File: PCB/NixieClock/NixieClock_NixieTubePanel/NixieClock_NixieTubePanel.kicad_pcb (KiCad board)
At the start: 2 copper layers, 112 x 112 mm, 30 parts, among them J3 Conn_01x04_Pin, J4 Conn_01x04_Pin, U1 K155ID1, U2 K155ID1, U3 K155ID1, U4 K155ID1, U5 PCF8574, U6 PCF8574, X1 5230, X2 5230, X3 5230, X4 5230, X5 5230, X6 5230

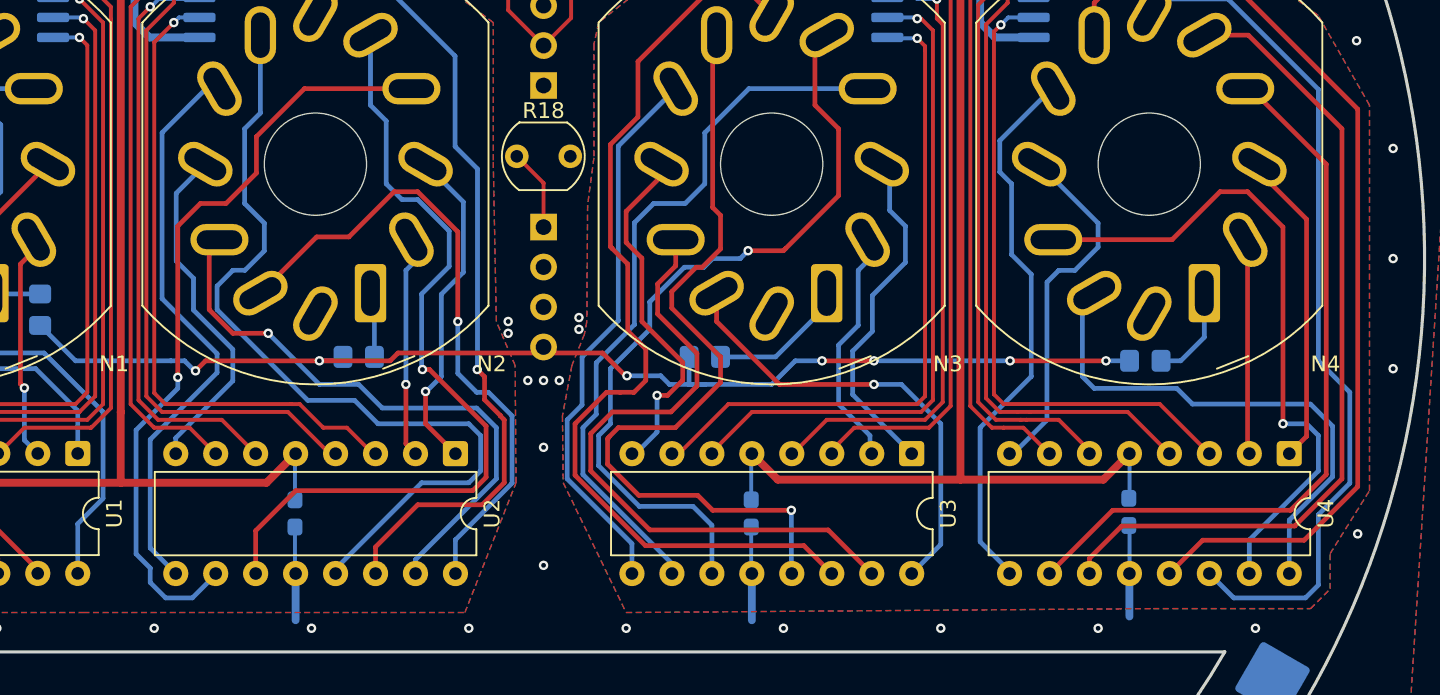
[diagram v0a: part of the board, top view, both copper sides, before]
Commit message: Tidied +170V trace slightly
some unnecessary diagonal lines were removed
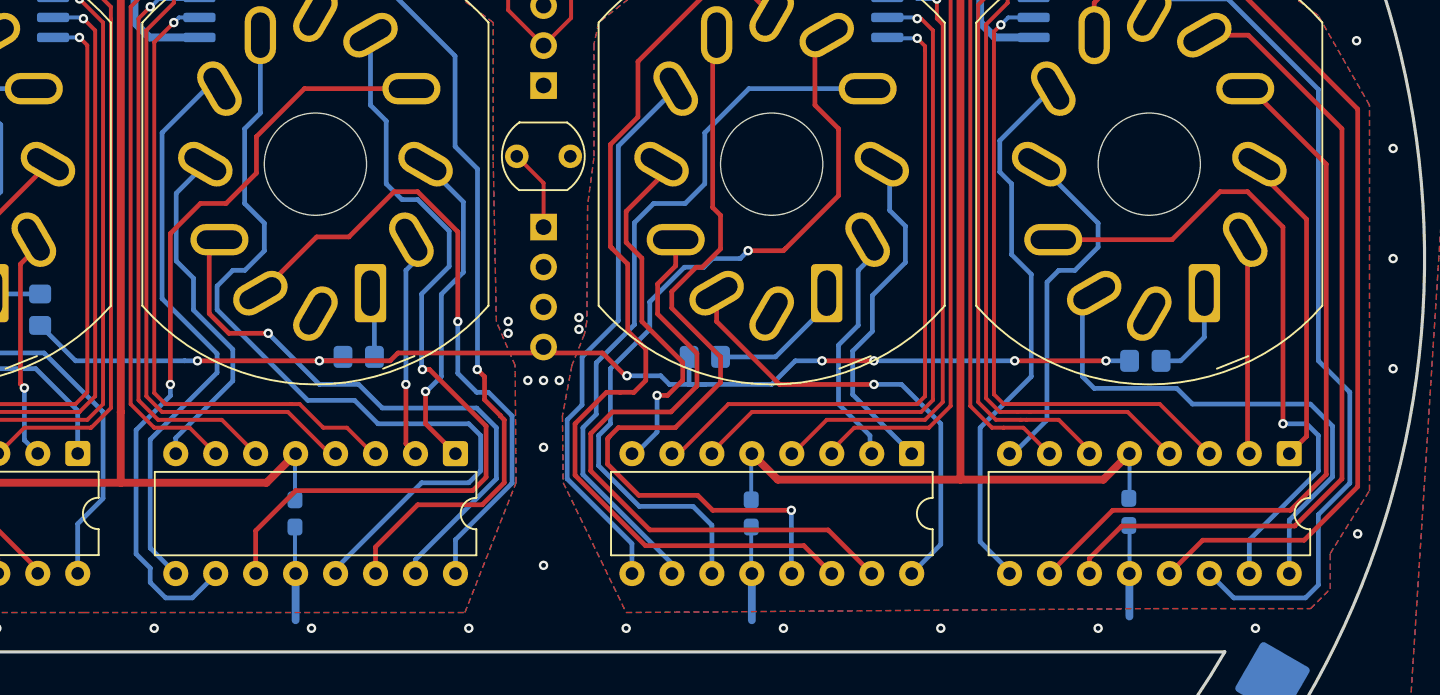
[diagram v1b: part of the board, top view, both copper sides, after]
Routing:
- net /+170V: track 78.5 -> 78.0 mm

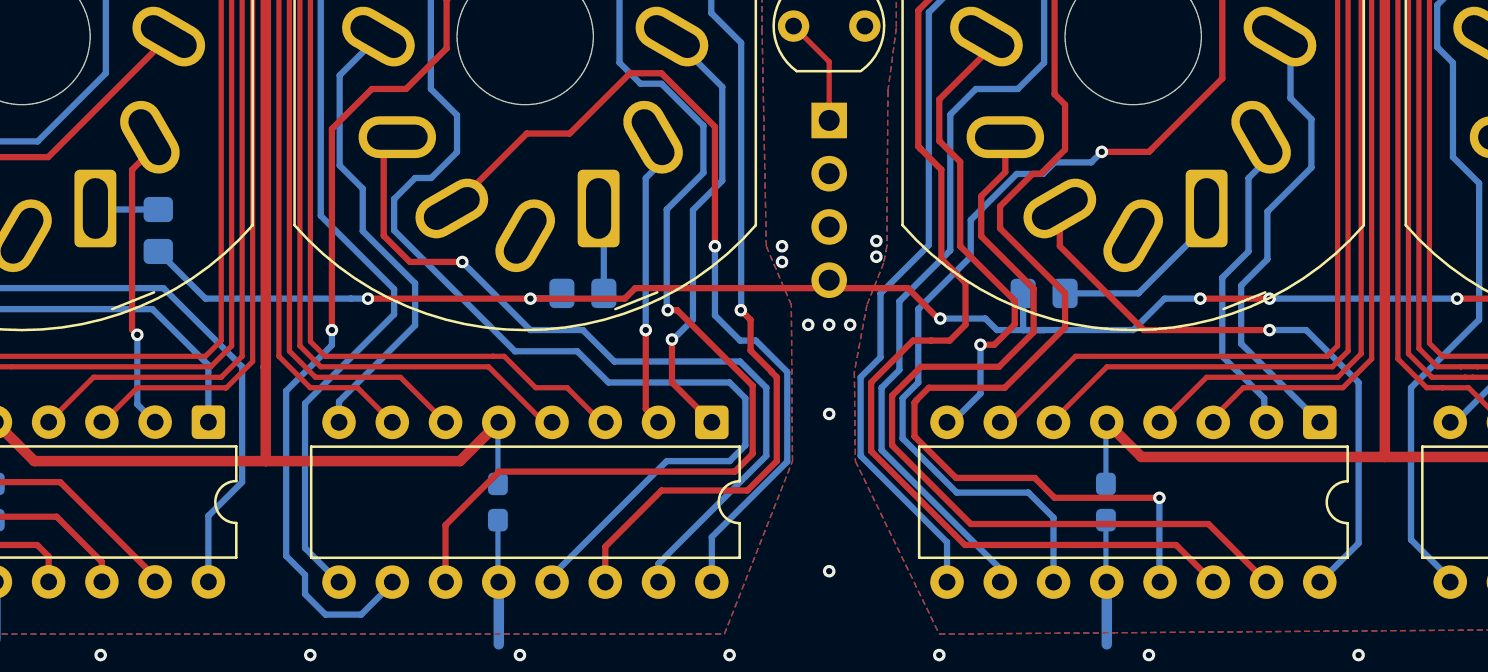
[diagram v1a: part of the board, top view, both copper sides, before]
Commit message: increase HV clearance on U3:8 trace
moved trace further from LV signals
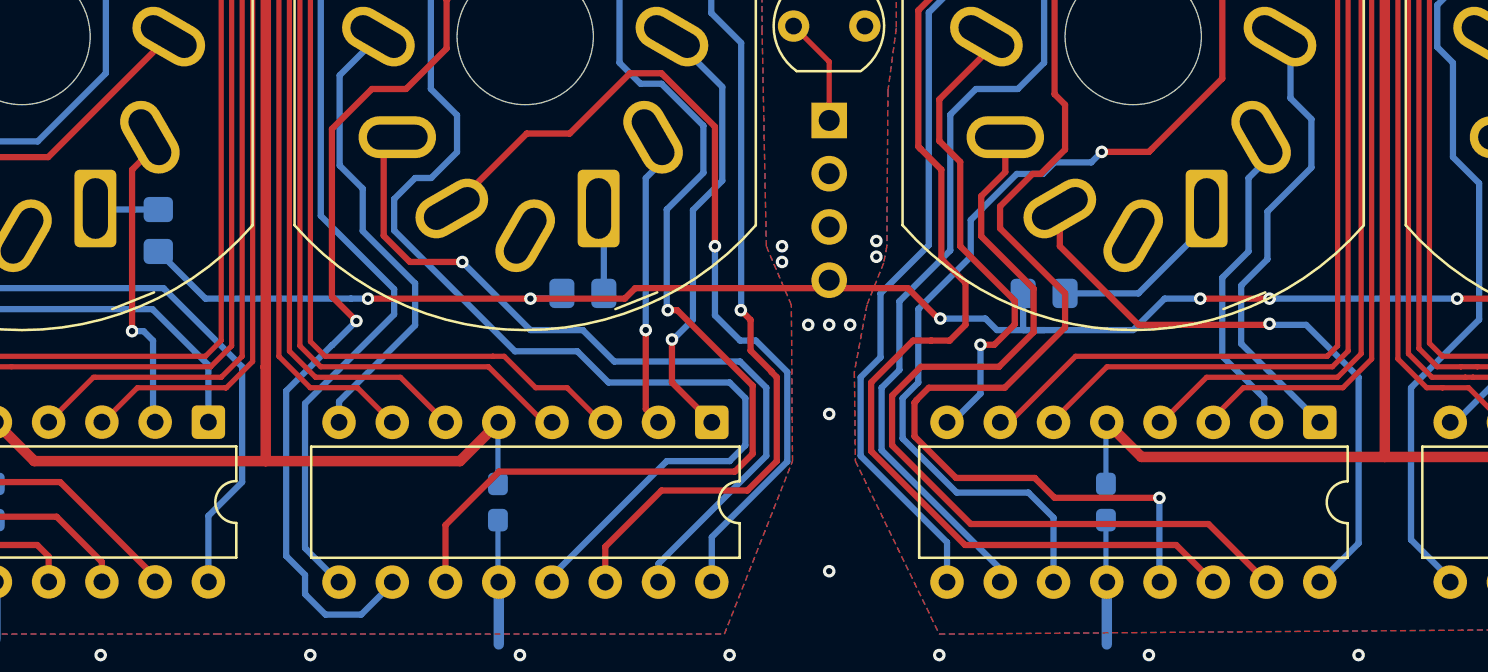
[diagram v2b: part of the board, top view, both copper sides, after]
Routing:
- net Net-(N2-'8'): track 49.3 -> 50.3 mm
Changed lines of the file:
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@@
 	)
 	(segment
-		(start 145 108)
+		(start 150.950003 107.75)
+		(end 144.75 107.75)
+		(width 0.3)
+		(layer "F.Cu")
+		(net 11)
+	)
+	(segment
+		(start 144.75 107.75)
 		(end 141 104)
 		(width 0.3)
@@
 	)
 	(segment
-		(start 151 108)
-		(end 145 108)
+		(start 151 107.700003)
+		(end 150.950003 107.75)
 		(width 0.3)
 		(layer "F.Cu")
@@
 	)
 	(via
-		(at 151 108)
+		(at 151 107.700003)
 		(size 0.6)
 		(drill 0.3)
@@
 	)
 	(segment
-		(start 152.75 108)
-		(end 155.25 110.5)
+		(start 155.25 118.17)
+		(end 153.4 120.02)
 		(width 0.3)
 		(layer "B.Cu")
@@
 	)
 	(segment
-		(start 155.25 118.17)
-		(end 153.4 120.02)
+		(start 155.25 110.25)
+		(end 155.25 118.17)
 		(width 0.3)
 		(layer "B.Cu")
@@
 	)
 	(segment
-		(start 155.25 110.5)
-		(end 155.25 118.17)
+		(start 152.75 107.75)
+		(end 155.25 110.25)
 		(width 0.3)
 		(layer "B.Cu")
@@
 	)
 	(segment
-		(start 151 108)
-		(end 152.75 108)
+		(start 151.049997 107.75)
+		(end 152.75 107.75)
+		(width 0.3)
+		(layer "B.Cu")
+		(net 11)
+	)
+	(segment
+		(start 151 107.700003)
+		(end 151.049997 107.75)
 		(width 0.3)
 		(layer "B.Cu")
@@
 	)
 	(segment
-		(start 97.6 99.501)
-		(end 97.6 98.8)
-		(width 0.3)
-		(layer "F.Cu")
-		(net 38)
-	)
-	(segment
-		(start 97 108.225)
-		(end 96.75 107.975)
+		(start 96.75 108.05)
+		(end 96.75 100.351)
 		(width 0.3)
 		(layer "F.Cu")
@@
 	)
 	(segment
-		(start 96.75 107.975)
-		(end 96.75 100.351)
+		(start 97.6 99.501)
+		(end 97.6 98.8)
 		(width 0.3)
 		(layer "F.Cu")
@@
 	)
 	(via
-		(at 97 108.225)
+		(at 96.75 108.05)
 		(size 0.6)
 		(drill 0.3)
@@
 	)
 	(segment
-		(start 97 111.54)
+		(start 97.75 112.29)
 		(end 97.85 112.39)
 		(width 0.3)
@@
 	)
 	(segment
-		(start 97 108.225)
-		(end 97 111.54)
+		(start 96.75 108.05)
+		(end 97.3 108.05)
+		(width 0.3)
+		(layer "B.Cu")
+		(net 38)
+	)
+	(segment
+		(start 97.3 108.05)
+		(end 97.75 108.5)
+		(width 0.3)
+		(layer "B.Cu")
+		(net 38)
+	)
+	(segment
+		(start 97.75 108.5)
+		(end 97.75 112.29)
 		(width 0.3)
 		(layer "B.Cu")
@@
 	)
 	(segment
-		(start 109.818507 96.5)
-		(end 111.75 94.568507)
+		(start 114.8 89.2)
+		(end 121.6 89.2)
 		(width 0.3)
 		(layer "F.Cu")
@@
 	)
 	(segment
-		(start 106.281 98.405856)
-		(end 108.186856 96.5)
+		(start 111.75 92.25)
+		(end 114.8 89.2)
 		(width 0.3)
 		(layer "F.Cu")
@@
 	)
 	(segment
-		(start 106.281 108)
-		(end 106.281 98.405856)
+		(start 111.75 94.568507)
+		(end 111.75 92.25)
 		(width 0.3)
 		(layer "F.Cu")
@@
 	)
 	(segment
-		(start 111.75 92.25)
-		(end 114.8 89.2)
+		(start 108.186856 96.5)
+		(end 109.818507 96.5)
 		(width 0.3)
 		(layer "F.Cu")
@@
 	)
 	(segment
-		(start 108.186856 96.5)
-		(end 109.818507 96.5)
+		(start 107.449035 107.566039)
+		(end 106.281 106.398004)
 		(width 0.3)
 		(layer "F.Cu")
@@
 	)
 	(segment
-		(start 111.75 94.568507)
-		(end 111.75 92.25)
+		(start 106.281 98.405856)
+		(end 108.186856 96.5)
 		(width 0.3)
 		(layer "F.Cu")
@@
 	)
 	(segment
-		(start 114.8 89.2)
-		(end 121.6 89.2)
+		(start 106.281 106.398004)
+		(end 106.281 98.405856)
+		(width 0.3)
+		(layer "F.Cu")
+		(net 56)
+	)
+	(segment
+		(start 109.818507 96.5)
+		(end 111.75 94.568507)
 		(width 0.3)
 		(layer "F.Cu")
@@
 	)
 	(via
-		(at 106.281 108)
+		(at 107.449035 107.566039)
 		(size 0.6)
 		(drill 0.3)
@@
 	)
 	(segment
-		(start 107.679 121.571)
-		(end 109.16 120.09)
+		(start 104.099 118.773206)
+		(end 105 119.674206)
+		(width 0.3)
+		(layer "B.Cu")
+		(net 56)
+	)
+	(segment
+		(start 107.449035 107.566039)
+		(end 106.296074 108.719)
 		(width 0.3)
 		(layer "B.Cu")
@@
 	)
 	(segment
-		(start 105 119.674206)
-		(end 105 120.593446)
+		(start 106.281 108.719)
+		(end 104.099 110.901)
 		(width 0.3)
 		(layer "B.Cu")
@@
 	)
 	(segment
-		(start 104.099 118.773206)
-		(end 105 119.674206)
+		(start 106.296074 108.719)
+		(end 106.281 108.719)
 		(width 0.3)
 		(layer "B.Cu")
@@
 	)
 	(segment
-		(start 104.099 110.901)
-		(end 104.099 118.773206)
+		(start 105 120.593446)
+		(end 105.977554 121.571)
 		(width 0.3)
 		(layer "B.Cu")
@@
 	)
 	(segment
-		(start 106.281 108)
-		(end 106.281 108.719)
+		(start 104.099 110.901)
+		(end 104.099 118.773206)
 		(width 0.3)
 		(layer "B.Cu")
@@
 	)
 	(segment
-		(start 106.281 108.719)
-		(end 104.099 110.901)
+		(start 105 119.674206)
+		(end 105 120.593446)
 		(width 0.3)
 		(layer "B.Cu")
@@
 	)
 	(segment
-		(start 105 120.593446)
-		(end 105.977554 121.571)
+		(start 107.679 121.571)
+		(end 109.16 120.09)
 		(width 0.3)
 		(layer "B.Cu")
